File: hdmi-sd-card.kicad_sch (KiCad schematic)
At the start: 33 parts, among them J4 HDMI-A_WE_685119134923, J5 MicroSD_693071020811, U10 TPD4E05U06QDQARQ1, U11 TPD4E05U06QDQARQ1, U12 TPD4E05U06QDQARQ1, U14 TPD4E05U06QDQARQ1

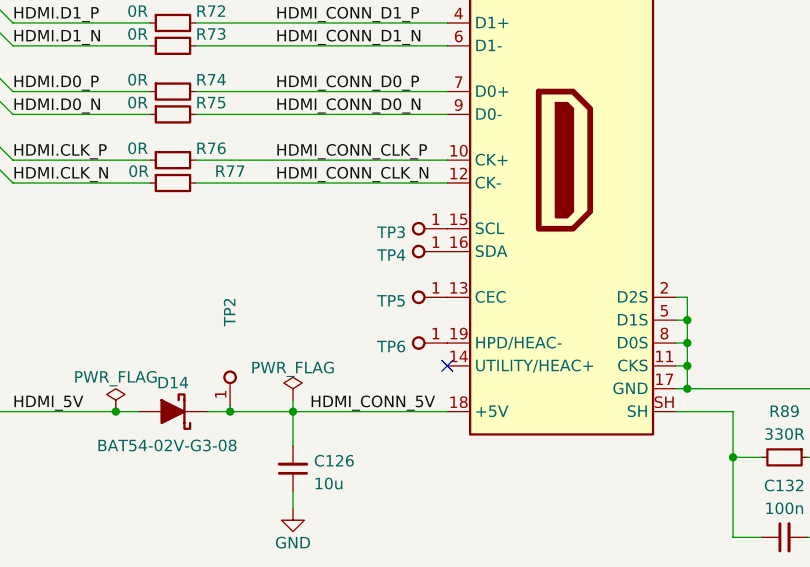
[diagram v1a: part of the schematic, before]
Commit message: Finish updating components to newest versions, improve silkscreen marking, bump revision
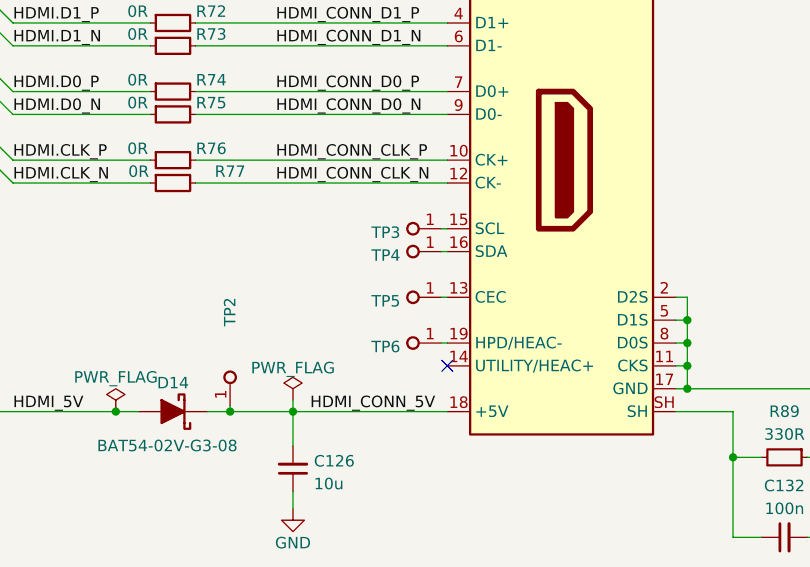
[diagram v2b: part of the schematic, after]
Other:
- moved on the sheet: TP3, TP4, TP5, TP6
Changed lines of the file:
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@@
     (title_block
         (title "SO-DIMM DDR5 Tester")
-        (date "2024-01-10")
-        (rev "1.1.0")
+        (date "2024-01-18")
+        (rev "1.1.1")
         (comment 1 "www.antmicro.com")
         (comment 2 "Antmicro Ltd"))
@@
     (wire
         (pts
+            (xy 225.425 186.69)
+            (xy 226.06 186.69))
+        (stroke
+            (width 0)
+            (type default)
+            (color 0 0 0 0))
+)
+    (wire
+        (pts
             (xy 269.24 212.09)
             (xy 266.065 212.09))
@@
     (wire
         (pts
+            (xy 225.425 194.31)
+            (xy 226.06 194.31))
+        (stroke
+            (width 0)
+            (type default)
+            (color 0 0 0 0))
+)
+    (wire
+        (pts
             (xy 186.055 88.9)
             (xy 184.785 88.9))
@@
             (color 0 0 0 0))
 )
+    (wire
+        (pts
+            (xy 225.425 199.39)
+            (xy 226.06 199.39))
+        (stroke
+            (width 0)
+            (type default)
+            (color 0 0 0 0))
+)
     (bus
         (pts
@@
     (wire
         (pts
+            (xy 225.425 189.23)
+            (xy 226.06 189.23))
+        (stroke
+            (width 0)
+            (type default)
+            (color 0 0 0 0))
+)
+    (wire
+        (pts
             (xy 177.8 109.22)
             (xy 186.055 109.22))
@@
     (symbol
         (lib_id "sodimm-ddr5-tester:TP_1mm_SMD")
-        (at 226.06 199.39 180)
+        (at 225.425 199.39 180)
         (unit 1)
         (in_bom yes)
@@
         (property "Reference" "TP6"
             (id 0)
-            (at 221.4881 199.8238 0)
+            (at 220.8531 199.8238 0)
             (effects
                 (font
@@
         (property "Value" "TP_1mm_SMD"
             (id 1)
-            (at 210.82 191.77 0)
+            (at 210.185 191.77 0)
             (effects
                 (font
@@
         (property "Footprint" "sodimm-ddr5-tester-footprints:TP_SMD_1mm"
             (id 2)
-            (at 210.82 189.23 0)
+            (at 210.185 189.23 0)
             (effects
                 (font
@@
         (property "Datasheet" ""
             (id 3)
-            (at 210.82 186.69 0)
+            (at 210.185 186.69 0)
             (effects
                 (font
@@
         (property "MPN" ""
             (id 4)
-            (at 226.06 199.39 0)
+            (at 225.425 199.39 0)
             (effects
                 (font
@@
         (property "Manufacturer" ""
             (id 5)
-            (at 226.06 199.39 0)
+            (at 225.425 199.39 0)
             (effects
                 (font
@@
         (property "Author" "Antmicro"
             (id 6)
-            (at 210.82 184.15 0)
+            (at 210.185 184.15 0)
             (effects
                 (font
@@
         (property "License" "Apache-2.0"
             (id 7)
-            (at 210.82 181.61 0)
+            (at 210.185 181.61 0)
             (effects
                 (font
@@
     (symbol
         (lib_id "sodimm-ddr5-tester:TP_1mm_SMD")
-        (at 226.06 194.31 180)
+        (at 225.425 194.31 180)
         (unit 1)
         (in_bom yes)
@@
         (property "Reference" "TP5"
             (id 0)
-            (at 221.4881 194.7438 0)
+            (at 220.8531 194.7438 0)
             (effects
                 (font
@@
         (property "Value" "TP_1mm_SMD"
             (id 1)
-            (at 210.82 186.69 0)
+            (at 210.185 186.69 0)
             (effects
                 (font
@@
         (property "Footprint" "sodimm-ddr5-tester-footprints:TP_SMD_1mm"
             (id 2)
-            (at 210.82 184.15 0)
+            (at 210.185 184.15 0)
             (effects
                 (font
@@
         (property "Datasheet" ""
             (id 3)
-            (at 210.82 181.61 0)
+            (at 210.185 181.61 0)
             (effects
                 (font
@@
         (property "MPN" ""
             (id 4)
-            (at 226.06 194.31 0)
+            (at 225.425 194.31 0)
             (effects
                 (font
@@
         (property "Manufacturer" ""
             (id 5)
-            (at 226.06 194.31 0)
+            (at 225.425 194.31 0)
             (effects
                 (font
@@
         (property "Author" "Antmicro"
             (id 6)
-            (at 210.82 179.07 0)
+            (at 210.185 179.07 0)
             (effects
                 (font
@@
         (property "License" "Apache-2.0"
             (id 7)
-            (at 210.82 176.53 0)
+            (at 210.185 176.53 0)
             (effects
                 (font
@@
     (symbol
         (lib_id "sodimm-ddr5-tester:TP_1mm_SMD")
-        (at 226.06 186.69 180)
+        (at 225.425 186.69 180)
         (unit 1)
         (in_bom yes)
@@
         (property "Reference" "TP3"
             (id 0)
-            (at 221.4881 187.1238 0)
+            (at 220.8531 187.1238 0)
             (effects
                 (font
@@
         (property "Value" "TP_1mm_SMD"
             (id 1)
-            (at 210.82 179.07 0)
+            (at 210.185 179.07 0)
             (effects
                 (font
@@
         (property "Footprint" "sodimm-ddr5-tester-footprints:TP_SMD_1mm"
             (id 2)
-            (at 210.82 176.53 0)
+            (at 210.185 176.53 0)
             (effects
                 (font
@@
         (property "Datasheet" ""
             (id 3)
-            (at 210.82 173.99 0)
+            (at 210.185 173.99 0)
             (effects
                 (font
@@
         (property "MPN" ""
             (id 4)
-            (at 226.06 186.69 0)
+            (at 225.425 186.69 0)
             (effects
                 (font
@@
         (property "Manufacturer" ""
             (id 5)
-            (at 226.06 186.69 0)
+            (at 225.425 186.69 0)
             (effects
                 (font
@@
         (property "Author" "Antmicro"
             (id 6)
-            (at 210.82 171.45 0)
+            (at 210.185 171.45 0)
             (effects
                 (font
@@
         (property "License" "Apache-2.0"
             (id 7)
-            (at 210.82 168.91 0)
+            (at 210.185 168.91 0)
             (effects
                 (font
@@
     (symbol
         (lib_id "sodimm-ddr5-tester:TP_1mm_SMD")
-        (at 226.06 189.23 180)
+        (at 225.425 189.23 180)
         (unit 1)
         (in_bom yes)
@@
         (property "Reference" "TP4"
             (id 0)
-            (at 221.4881 189.6638 0)
+            (at 220.8531 189.6638 0)
             (effects
                 (font
@@
         (property "Value" "TP_1mm_SMD"
             (id 1)
-            (at 210.82 181.61 0)
+            (at 210.185 181.61 0)
             (effects
                 (font
@@
         (property "Footprint" "sodimm-ddr5-tester-footprints:TP_SMD_1mm"
             (id 2)
-            (at 210.82 179.07 0)
+            (at 210.185 179.07 0)
             (effects
                 (font
@@
         (property "Datasheet" ""
             (id 3)
-            (at 210.82 176.53 0)
+            (at 210.185 176.53 0)
             (effects
                 (font
@@
         (property "MPN" ""
             (id 4)
-            (at 226.06 189.23 0)
+            (at 225.425 189.23 0)
             (effects
                 (font
@@
         (property "Manufacturer" ""
             (id 5)
-            (at 226.06 189.23 0)
+            (at 225.425 189.23 0)
             (effects
                 (font
@@
         (property "Author" "Antmicro"
             (id 6)
-            (at 210.82 173.99 0)
+            (at 210.185 173.99 0)
             (effects
                 (font
@@
         (property "License" "Apache-2.0"
             (id 7)
-            (at 210.82 171.45 0)
+            (at 210.185 171.45 0)
             (effects
                 (font

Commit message: Finish schematic cleanup
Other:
- moved on the sheet: U10, U11

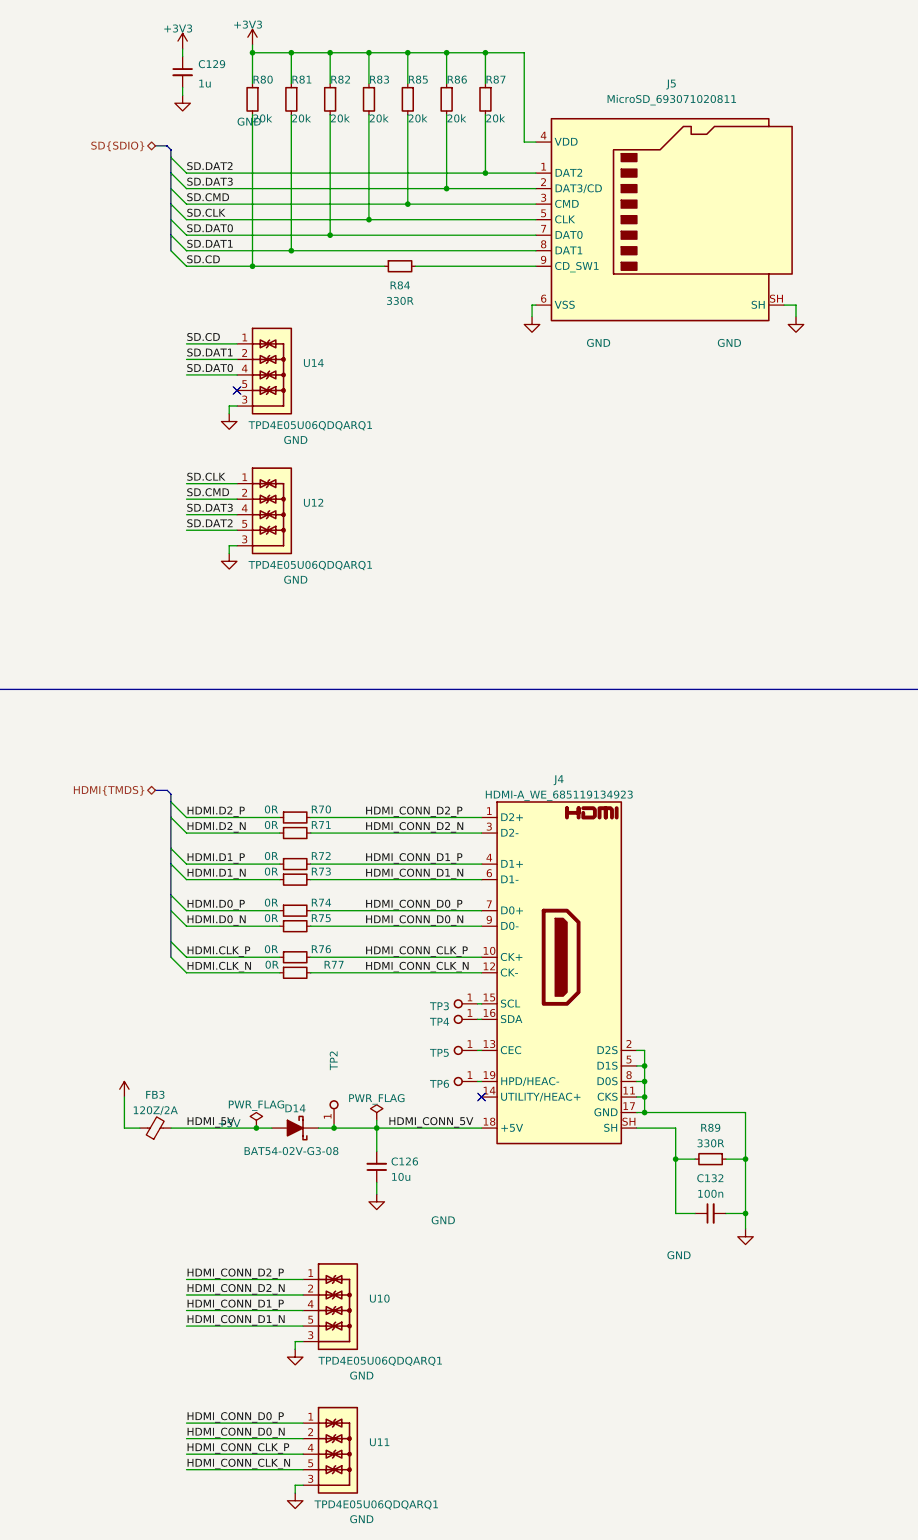
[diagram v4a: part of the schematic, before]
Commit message: Add updated components to local library
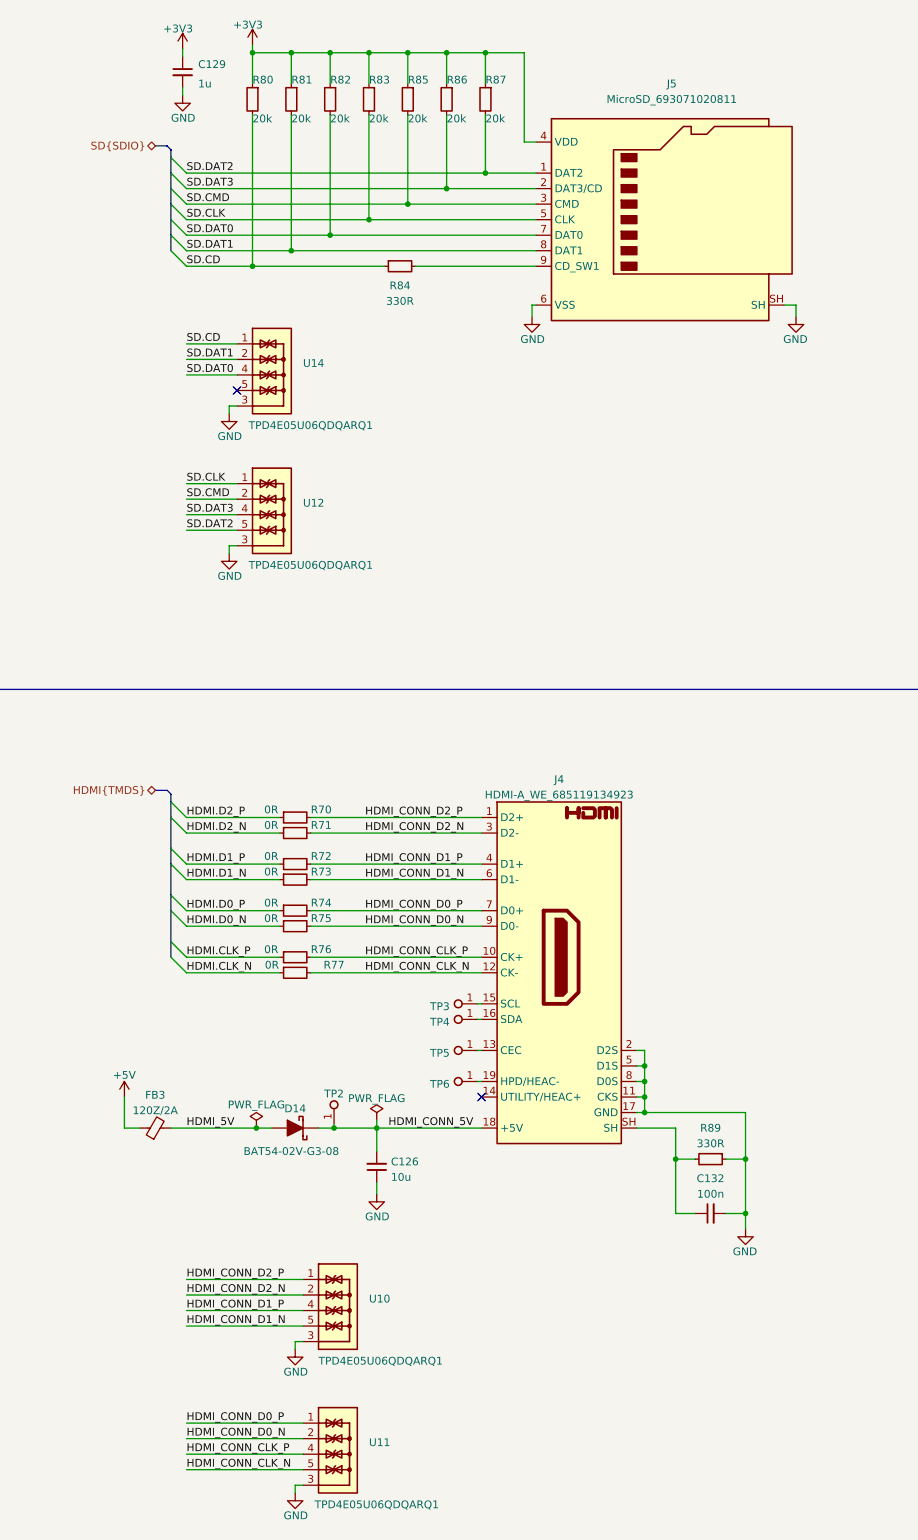
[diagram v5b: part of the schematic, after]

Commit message: [#57478] ohp release
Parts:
- C126: footprint sodimm-ddr5-tester-footprints:C_0402_1005Metric -> antmicro-footprints:C_0402_1005Metric; symbol sodimm-ddr5-tester:C_10u_6.3V_0402 -> antmicroCapacitors0402:C_10u_6.3V_0402
- C129: footprint sodimm-ddr5-tester-footprints:C_0402_1005Metric -> antmicro-footprints:C_0402_1005Metric; symbol sodimm-ddr5-tester:C_1u_0402 -> antmicroCapacitors0402:C_1u_0402
- C132: footprint sodimm-ddr5-tester-footprints:C_0402_1005Metric -> antmicro-footprints:C_0402_1005Metric; symbol sodimm-ddr5-tester:C_100n_0402 -> antmicroCapacitors0402:C_100n_0402
- D14: footprint sodimm-ddr5-tester-footprints:SOD-523 -> antmicro-footprints:SOD-523; symbol sodimm-ddr5-tester:BAT54-02V-G3-08 -> antmicroDiodesRectifiersSingle:BAT54-02V-G3-08
- FB3: footprint sodimm-ddr5-tester-footprints:FB_0603_1608Metric -> antmicro-footprints:FB_0603_1608Metric; symbol sodimm-ddr5-tester:FB_120Z_2A_Murata-BLM18PG_0603 -> antmicroFerriteBeadsandChips:FB_120Z_2A_Murata-BLM18PG_0603
- J4: footprint sodimm-ddr5-tester-footprints:HDMI-A_Receptacle_WE_685119134923 -> antmicro-footprints:HDMI-A_Receptacle_WE_685119134923; symbol sodimm-ddr5-tester:HDMI-A_WE_685119134923 -> antmicroVideoConnectors:HDMI-A_WE_685119134923
- J5: footprint sodimm-ddr5-tester-footprints:MicroSD_Wurth_693071020811 -> antmicro-footprints:MicroSD_Wurth_693071020811; symbol sodimm-ddr5-tester:MicroSD_693071020811 -> antmicroMemoryConnectorsPCCardSockets:MicroSD_693071020811
- R70, R71, R72, R73, R74, R75, R76, R77: footprint sodimm-ddr5-tester-footprints:R_0402_1005Metric -> antmicro-footprints:R_0402_1005Metric; symbol sodimm-ddr5-tester:R_0R_0402 -> antmicroResistors0402:R_0R_0402
- R80, R81, R82, R83, R85, R86, R87: footprint sodimm-ddr5-tester-footprints:R_0402_1005Metric -> antmicro-footprints:R_0402_1005Metric; symbol sodimm-ddr5-tester:R_20k_0402 -> antmicroResistors0402:R_20k_0402
- R84, R89: footprint sodimm-ddr5-tester-footprints:R_0402_1005Metric -> antmicro-footprints:R_0402_1005Metric; symbol sodimm-ddr5-tester:R_330R_0402 -> antmicroResistors0402:R_330R_0402
- TP2, TP3, TP4, TP5, TP6: footprint sodimm-ddr5-tester-footprints:TP_SMD_1mm -> antmicro-footprints:TP_SMD_1mm; symbol sodimm-ddr5-tester:TP_1mm_SMD -> antmicroTestPoints:TP_1mm_SMD
- U10, U11, U12, U14: footprint sodimm-ddr5-tester-footprints:USON-10_2.5x1mm_P0.5mm -> antmicro-footprints:USON-10_2.5x1mm_P0.5mm; symbol sodimm-ddr5-tester:TPD4E05U06QDQARQ1 -> antmicroTVSDiodes:TPD4E05U06QDQARQ1
